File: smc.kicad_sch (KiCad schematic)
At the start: 29 parts

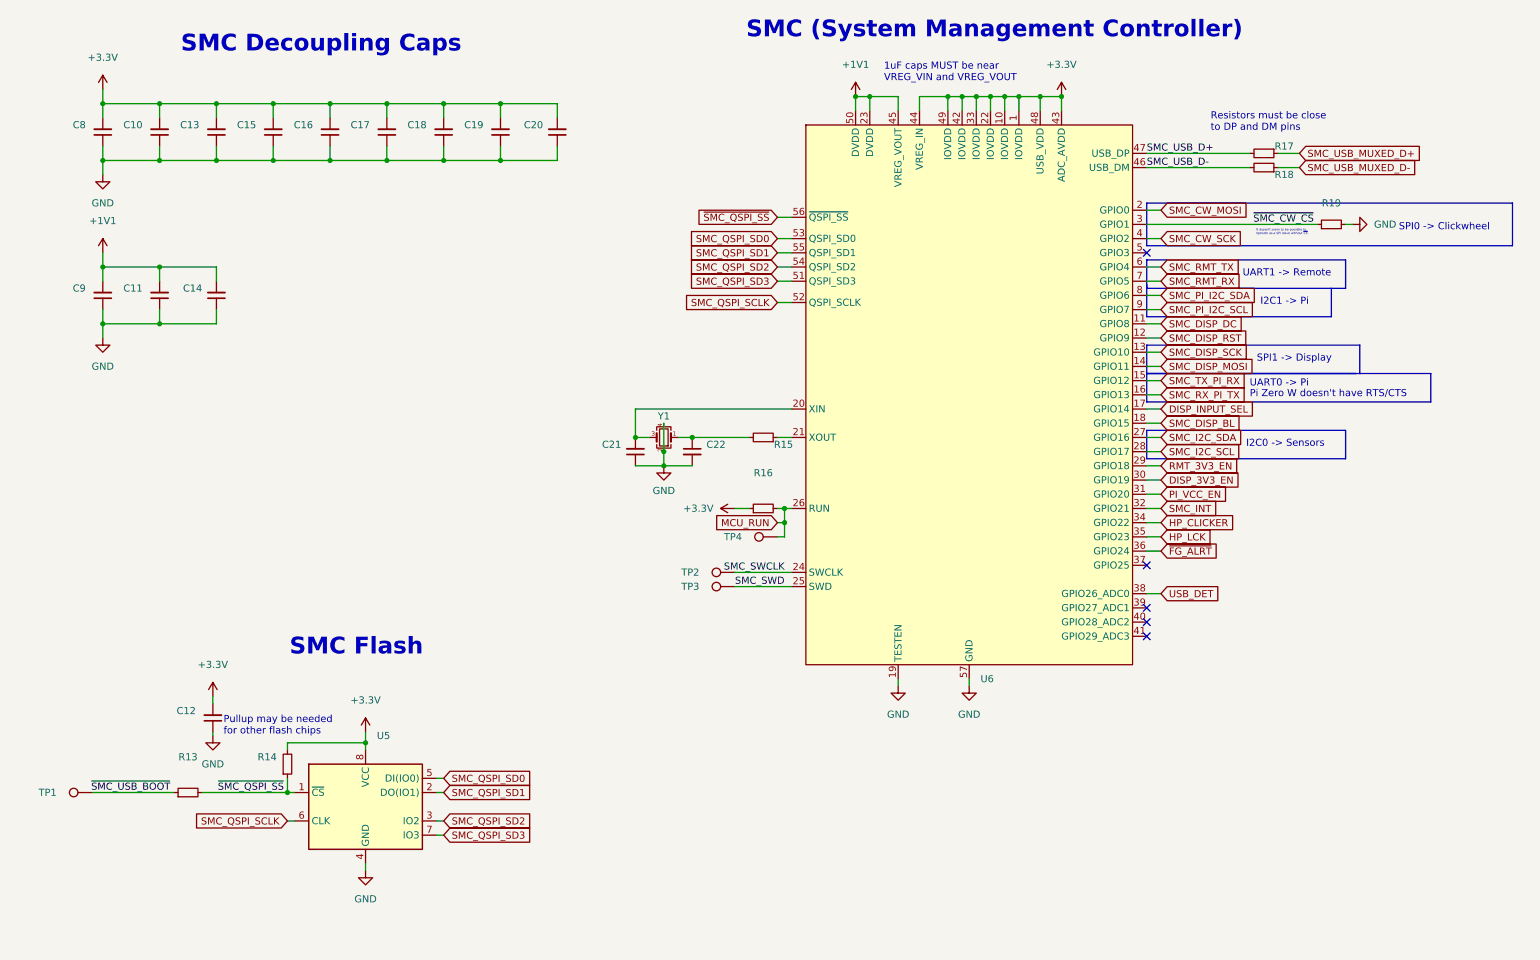
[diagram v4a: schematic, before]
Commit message: layout: update footprint for TP4056M
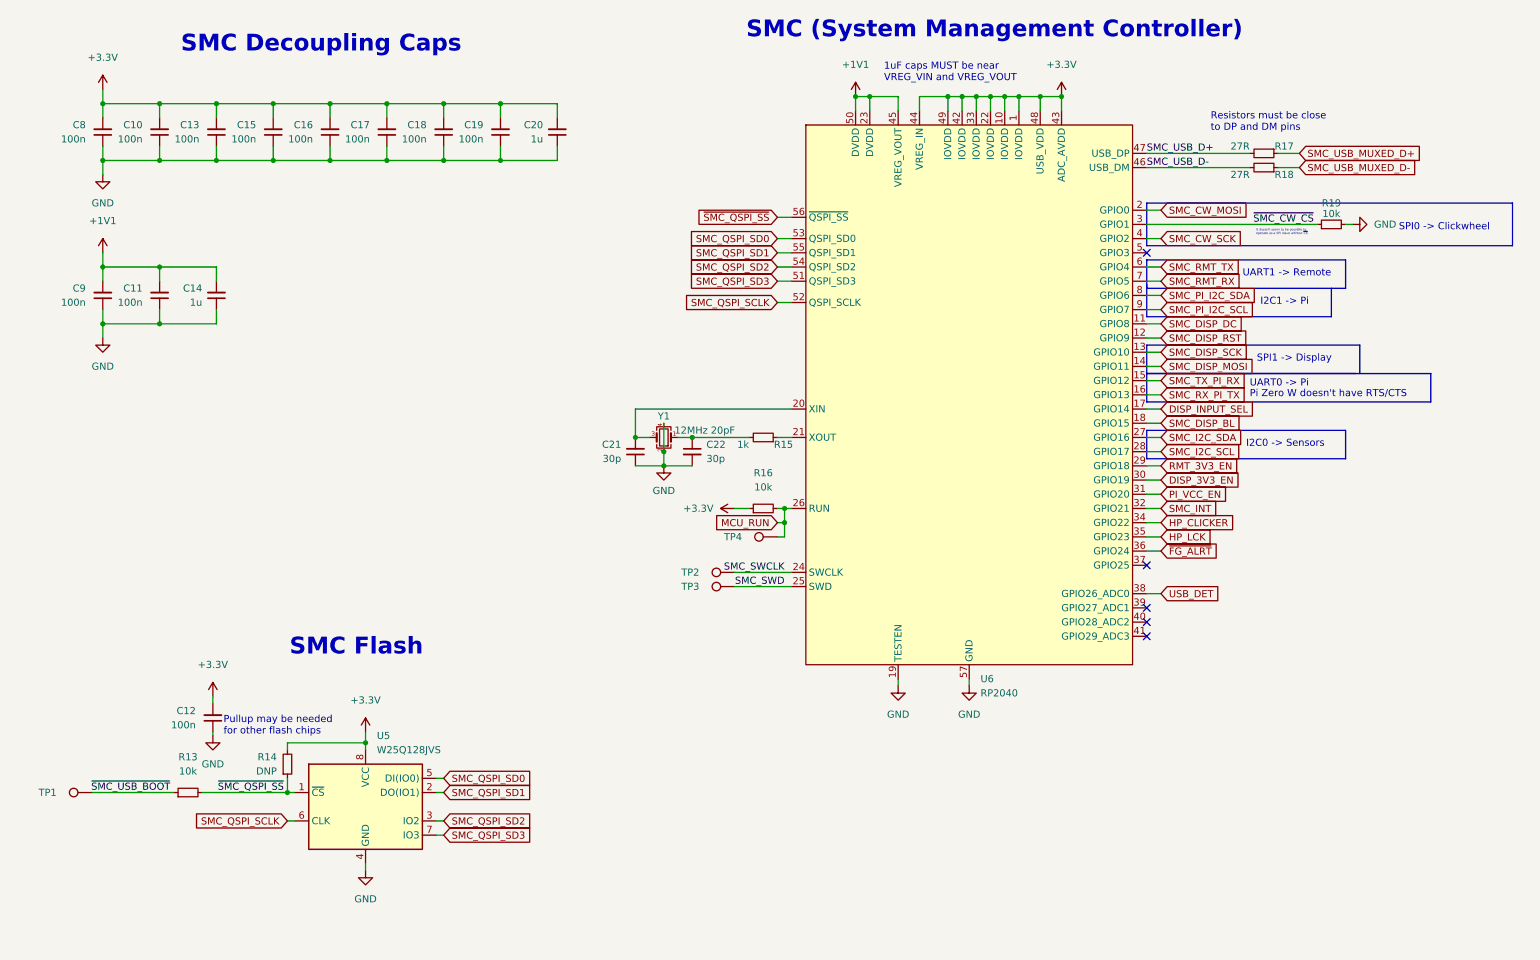
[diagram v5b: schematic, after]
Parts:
- C10, C11, C12, C13, C15, C16, C17, C18, C19, C8, C9: value (none) -> 100n; footprint (none) -> Capacitor_SMD:C_0402_1005Metric
- C14, C20: value (none) -> 1u; footprint (none) -> Capacitor_SMD:C_0402_1005Metric
- C21, C22: value (none) -> 30p; footprint (none) -> Capacitor_SMD:C_0402_1005Metric
- R13, R16, R19: value (none) -> 10k; footprint (none) -> Resistor_SMD:R_0402_1005Metric
- R14: value (none) -> DNP; footprint (none) -> Resistor_SMD:R_0402_1005Metric
- R15: value (none) -> 1k; footprint (none) -> Resistor_SMD:R_0402_1005Metric
- R17, R18: value (none) -> 27R; footprint (none) -> Resistor_SMD:R_0402_1005Metric
- TP1, TP2, TP3, TP4: value (none) -> TestPoint; footprint (none) -> TestPoint:TestPoint_Pad_D1.5mm
- U5: value (none) -> W25Q128JVS; footprint (none) -> Package_SO:SOIC-8_5.23x5.23mm_P1.27mm
- U6: value (none) -> RP2040; footprint (none) -> Package_DFN_QFN:QFN-56-1EP_7x7mm_P0.4mm_EP5.6x5.6mm
- Y1: value (none) -> 12MHz 20pF; footprint (none) -> Crystal:Crystal_SMD_3225-4Pin_3.2x2.5mm

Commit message: layout: preliminary layout of most of board
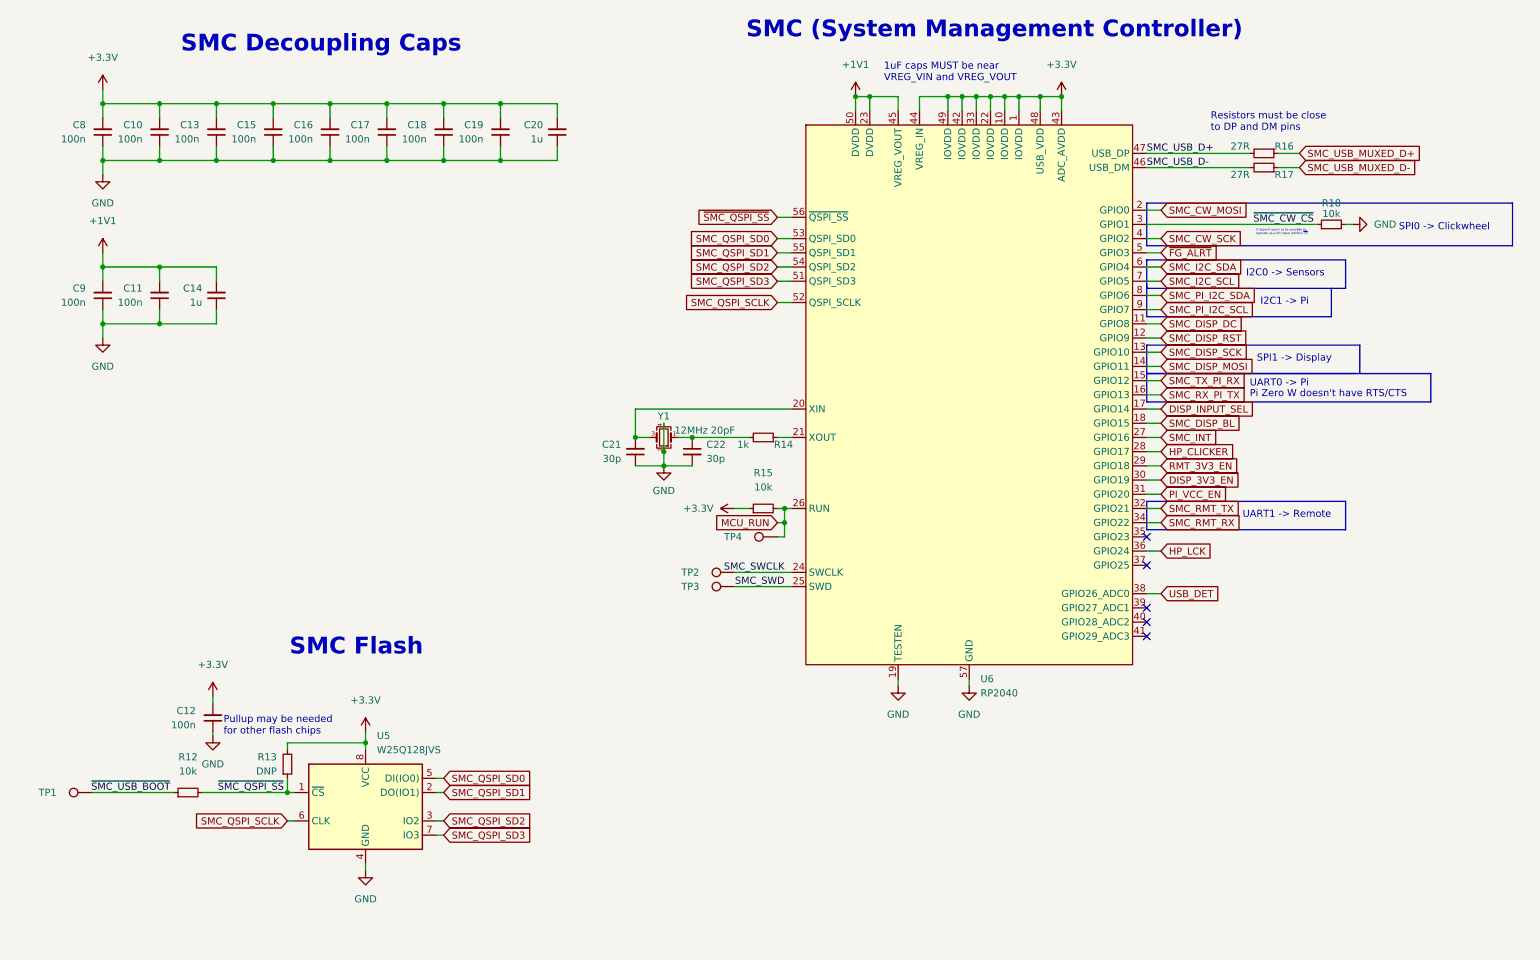
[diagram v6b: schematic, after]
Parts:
- renumbered R13 to R12, R14 to R13, R15 to R14, R16 to R15, R17 to R16, R18 to R17, R19 to R18
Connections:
- net HP_CLICKER: now also U6.28 (GPIO17); no longer U6.34 (GPIO22)
- net HP_LCK: now also U6.36 (GPIO24); no longer U6.35 (GPIO23)
- net SMC_I2C_SCL: now also U6.7 (GPIO5); no longer U6.28 (GPIO17)
- net SMC_I2C_SDA: now also U6.6 (GPIO4); no longer U6.27 (GPIO16)
- net SMC_INT: now also U6.27 (GPIO16); no longer U6.32 (GPIO21)
- net SMC_RMT_RX: now also U6.34 (GPIO22); no longer U6.7 (GPIO5)
- net SMC_RMT_TX: now also U6.32 (GPIO21); no longer U6.6 (GPIO4)
- net ~{FG_ALRT}: now also U6.5 (GPIO3); no longer U6.36 (GPIO24)

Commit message: routing: begin routing
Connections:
- net DISP_INPUT_SEL: now also U6.39 (GPIO27_ADC1); no longer U6.17 (GPIO14)
- net SMC_DISP_BL: now also U6.40 (GPIO28_ADC2); no longer U6.18 (GPIO15)
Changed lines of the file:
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@@
   (no_connect (at 217.17 121.92))
   (no_connect (at 217.17 139.7))
-  (no_connect (at 217.17 137.16))
-  (no_connect (at 217.17 134.62))
+  (no_connect (at 217.17 101.6))
+  (no_connect (at 217.17 99.06))
   (wire (pts (xy 217.17 93.98) (xy 219.71 93.98))
     (stroke (width 0) (type default) (color 0 0 0 0))
@@
     (stroke (width 0) (type default) (color 0 0 0 0))
   )
+  (wire (pts (xy 217.17 137.16) (xy 219.71 137.16))
+    (stroke (width 0) (type default) (color 0 0 0 0))
+  )
   (wire (pts (xy 185.42 147.32) (xy 185.42 148.59))
     (stroke (width 0) (type default) (color 0 0 0 0))
@@
     (stroke (width 0) (type default) (color 0 0 0 0))
   )
-  (wire (pts (xy 217.17 101.6) (xy 219.71 101.6))
-    (stroke (width 0) (type default) (color 0 0 0 0))
-  )
   (wire (pts (xy 30.48 83.82) (xy 30.48 86.36))
     (stroke (width 0) (type default) (color 0 0 0 0))
@@
     (stroke (width 0) (type default) (color 0 0 0 0))
   )
-  (wire (pts (xy 217.17 99.06) (xy 219.71 99.06))
+  (wire (pts (xy 217.17 134.62) (xy 219.71 134.62))
     (stroke (width 0) (type default) (color 0 0 0 0))
   )
@@
     (effects (font (size 1.27 1.27)) (justify right bottom))
   )
-  (global_label "SMC_DISP_BL" (shape input) (at 219.71 101.6 0) (fields_autoplaced)
-    (effects (font (size 1.27 1.27)) (justify left))
-    (property "Intersheet References" "${INTERSHEET_REFS}" (id 0) (at 234.6417 101.6794 0)
+  (global_label "SMC_DISP_BL" (shape input) (at 219.71 137.16 0) (fields_autoplaced)
+    (effects (font (size 1.27 1.27)) (justify left))
+    (property "Intersheet References" "${INTERSHEET_REFS}" (id 0) (at 234.6417 137.2394 0)
       (effects (font (size 1.27 1.27)) (justify left) hide)
     )
@@
     )
   )
-  (global_label "DISP_INPUT_SEL" (shape input) (at 219.71 99.06 0) (fields_autoplaced)
-    (effects (font (size 1.27 1.27)) (justify left))
-    (property "Intersheet References" "${INTERSHEET_REFS}" (id 0) (at 237.3026 98.9806 0)
-      (effects (font (size 1.27 1.27)) (justify left) hide)
-    )
+  (global_label "DISP_INPUT_SEL" (shape input) (at 219.71 134.62 0) (fields_autoplaced)
+    (effects (font (size 1.27 1.27)) (justify left))
+    (property "Intersheet References" "${INTERSHEET_REFS}" (id 0) (at 237.3026 134.5406 0)
+      (effects (font (size 1.27 1.27)) (justify left) hide)
+    )

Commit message: layout, routing: relayout and reroute board
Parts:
- added R46, R47: (no value), symbol Device:R_Small
- C10, C11, C12, C13, C15, C16, C17, C18, C19, C8, C9: value 100n -> (none); footprint Capacitor_SMD:C_0402_1005Metric -> (none)
- C14, C20: value 1u -> (none); footprint Capacitor_SMD:C_0402_1005Metric -> (none)
- C21, C22: value 30p -> (none); footprint Capacitor_SMD:C_0402_1005Metric -> (none)
- R12, R15, R18: value 10k -> (none); footprint Resistor_SMD:R_0402_1005Metric -> (none)
- R13: value DNP -> (none); footprint Resistor_SMD:R_0402_1005Metric -> (none)
- R14: value 1k -> (none); footprint Resistor_SMD:R_0402_1005Metric -> (none)
- R16, R17: value 27R -> (none); footprint Resistor_SMD:R_0402_1005Metric -> (none)
- TP1, TP2, TP3, TP4: value TestPoint -> (none); footprint TestPoint:TestPoint_Pad_D1.5mm -> (none)
- U5: value W25Q128JVS -> (none); footprint Package_SO:SOIC-8_5.23x5.23mm_P1.27mm -> (none); symbol Memory_Flash:W25Q128JVS -> gigahawk:W25Q128JVP
- U6: value RP2040 -> (none); footprint Package_DFN_QFN:QFN-56-1EP_7x7mm_P0.4mm_EP5.6x5.6mm -> (none)
- Y1: value 12MHz 20pF -> (none); footprint Crystal:Crystal_SMD_3225-4Pin_3.2x2.5mm -> (none); Digikey Part (none) -> FH1200001CT-ND; Digikey Price/Stock (none) -> https://www.digikey.ca/en/products/detail/diodes-incorporat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; JLC Part (none) -> Extended Part; LCSC Part (none) -> C1985748; Manufacturer (none) -> Diodes Incorporated; Manufacturer Part (none) -> FH1200001; Mouser Part (none) -> 729-FH1200001; Mouser Price/Stock (none) -> https://www.mouser.ca/ProductDetail/Diodes-Incorporated/FH1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
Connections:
- net +3V3: now also R46.1, R47.1
- net DISP_3V3_EN: now also U6.18 (GPIO15); no longer U6.30 (GPIO19)
- net DISP_INPUT_SEL: now also U6.27 (GPIO16); no longer U6.39 (GPIO27_ADC1)
- net HP_CLICKER: now also U6.13 (GPIO10); no longer U6.28 (GPIO17)
- net HP_LCK: now also U6.14 (GPIO11); no longer U6.36 (GPIO24)
- net PI_VCC_EN: now also U6.2 (GPIO0); no longer U6.31 (GPIO20)
- net RMT_3V3_EN: now also U6.36 (GPIO24); no longer U6.29 (GPIO18)
- net SMC_CW_MOSI: now also U6.40 (GPIO28_ADC2); no longer U6.2 (GPIO0)
- net SMC_CW_SCK: now also U6.38 (GPIO26_ADC0); no longer U6.4 (GPIO2)
- net SMC_DISP_BL: now also U6.32 (GPIO21); no longer U6.40 (GPIO28_ADC2)
- net SMC_DISP_DC: now also U6.31 (GPIO20); no longer U6.11 (GPIO8)
- net SMC_DISP_MOSI: now also U6.30 (GPIO19); no longer U6.14 (GPIO11)
- net SMC_DISP_RST: now also U6.28 (GPIO17); no longer U6.12 (GPIO9)
- net SMC_DISP_SCK: now also U6.29 (GPIO18); no longer U6.13 (GPIO10)
- net SMC_I2C_SCL: now also U6.35 (GPIO23), R47.2; no longer U6.7 (GPIO5)
- net SMC_I2C_SDA: now also U6.34 (GPIO22), R46.2; no longer U6.6 (GPIO4)
- net SMC_INT: now also U6.3 (GPIO1); no longer U6.27 (GPIO16)
- net SMC_PI_I2C_SCL: now also U6.12 (GPIO9); no longer U6.9 (GPIO7)
- net SMC_PI_I2C_SDA: now also U6.11 (GPIO8); no longer U6.8 (GPIO6)
- net SMC_RMT_RX: now also U6.16 (GPIO13); no longer U6.34 (GPIO22)
- net SMC_RMT_TX: now also U6.15 (GPIO12); no longer U6.32 (GPIO21)
- net SMC_RX_PI_TX: now also U6.6 (GPIO4); no longer U6.16 (GPIO13)
- net SMC_TX_PI_RX: now also U6.7 (GPIO5); no longer U6.15 (GPIO12)
- net USB_DET: now also U6.41 (GPIO29_ADC3); no longer U6.38 (GPIO26_ADC0)
- net ~{FG_ALRT}: now also U6.39 (GPIO27_ADC1); no longer U6.5 (GPIO3)
- net ~{SMC_CW_CS}: now also U6.37 (GPIO25); no longer U6.3 (GPIO1)
- net SMC_XIN: now reaches C21.2, U6.20 (XIN), Y1.3
- net SMC_XOUT_ATTN: now reaches C22.1, R14.2, Y1.1
- net SMC_XOUT: now reaches R14.1, U6.21 (XOUT)
- new net USB_MUX_SEL: U6.4 (GPIO2)
- no-connect marks 5 -> 4
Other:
- note added: "I2C Pullups"
- note added: "I2C0 -> Pi"
- note added: "I2C1 -> Sensors"
- note added: "Pi contains its own resistor pullups, exxternal pullups only needed for SMC bus"
- note added: "SPI0 -> Display"
- note added: "SPI1 -> Clickwheel"
- note added: "UART0 -> Remote"
- note added: "UART1 -> Pi"
- note removed: "I2C0 -> Sensors"
- note removed: "I2C1 -> Pi"
- note removed: "SPI0 -> Clickwheel"
- note removed: "SPI1 -> Display"
- note removed: "UART0 -> Pi"
- note removed: "UART1 -> Remote"
- moved on the sheet: C12, C21, C22, R12, R13, R14, R18, TP1, U5, Y1
